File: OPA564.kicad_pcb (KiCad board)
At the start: 2 copper layers, 57.5 x 55 mm, 15 parts, among them IC1 OPA564AIDWD, J1 Conn_Coaxial, J2 Conn_Coaxial

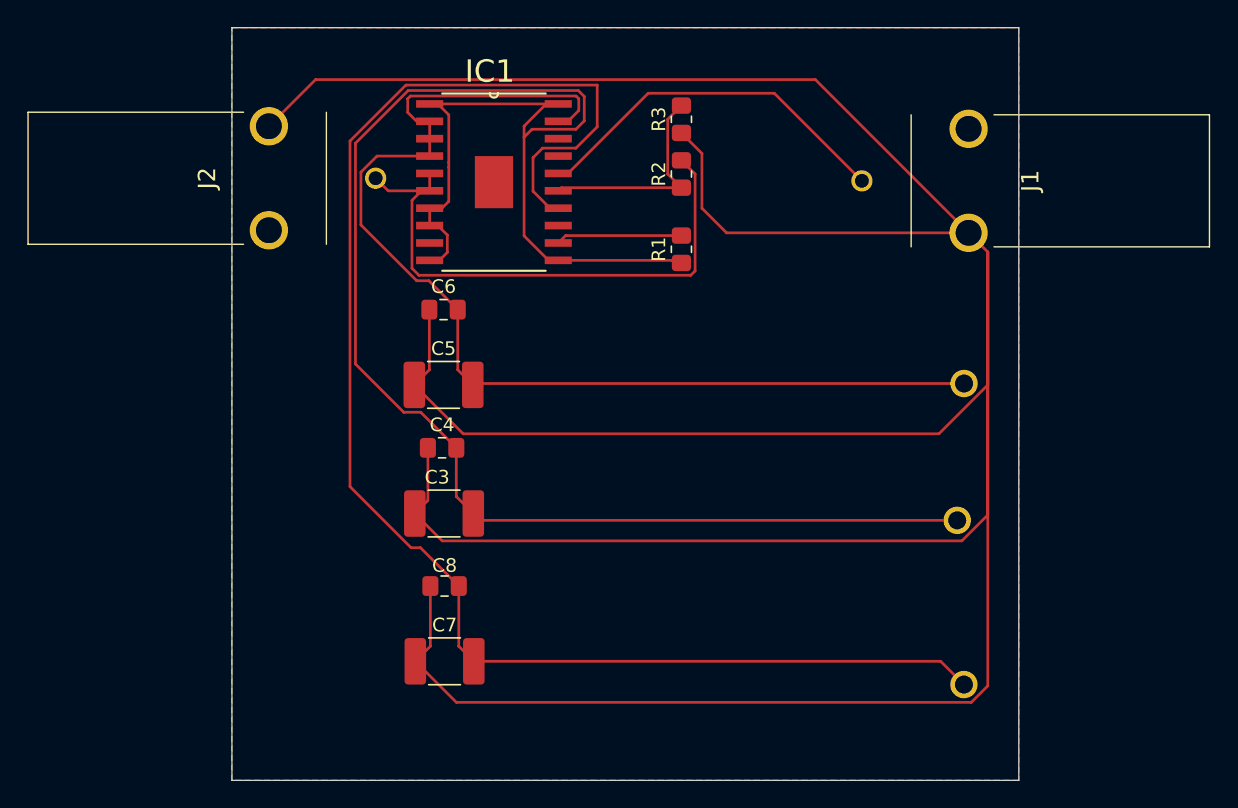
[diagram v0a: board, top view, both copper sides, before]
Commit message: OPA564 simplest design
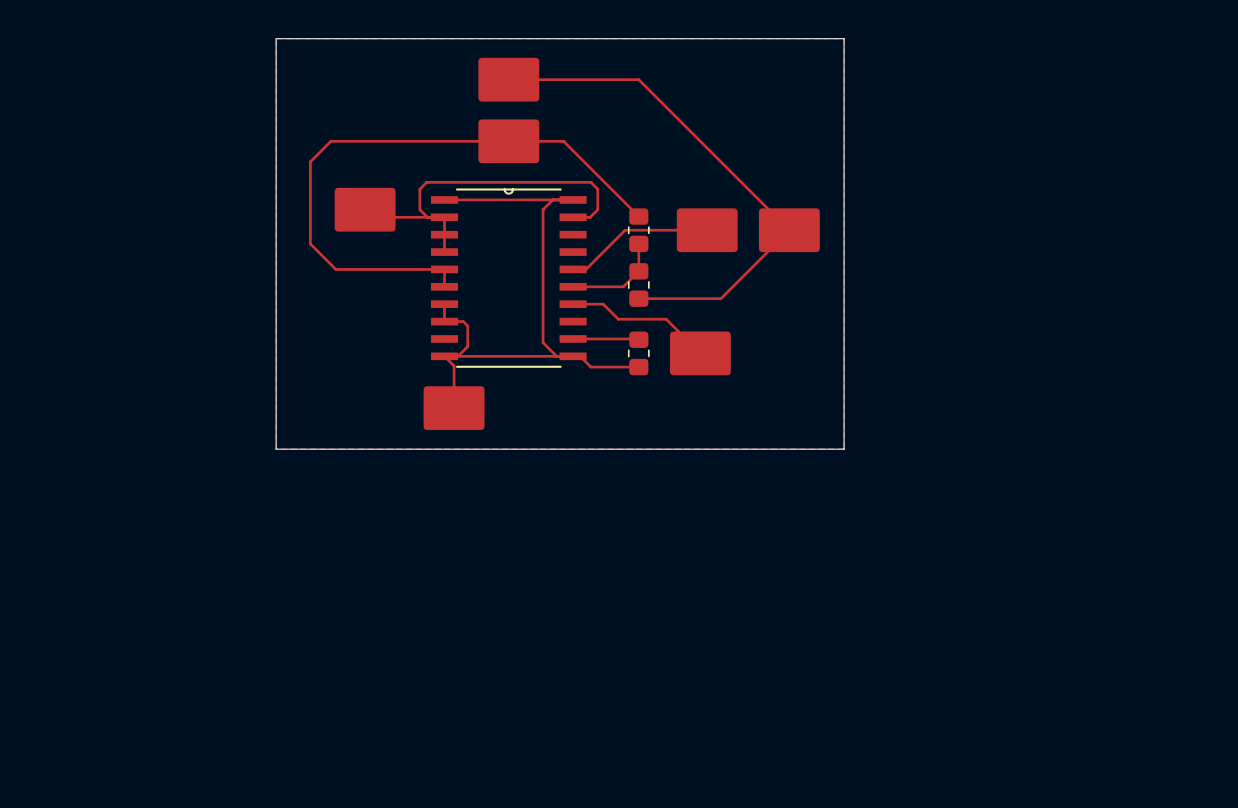
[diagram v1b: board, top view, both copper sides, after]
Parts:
- removed the ? at (169.8, 74.7)
- removed the ? at (169.8, 96.7)
- removed the ? at (169.3, 84.7)
- removed C3, C5, C7: 47 uC, Capacitor_SMD:C_1812_4532Metric_Pad1.57x3.40mm_HandSolder
- removed C4, C6, C8: 0.1 uC, Capacitor_SMD:C_0805_2012Metric_Pad1.18x1.45mm_HandSolder
- removed J1, J2: Conn_Coaxial, 731000154:731000154
- added ?: , , F.Cu at (150.5, 72.5)
- added ?: , , F.Cu at (157.0, 63.5)
- added ?: , , F.Cu at (136.5, 57.0)
- added ?: , , F.Cu at (136.5, 52.5)
- added ?: , , F.Cu at (126.0, 62.0)
- added ?: , , F.Cu at (151.0, 63.5)
- added ?: , , F.Cu at (132.5, 76.5)
- R1: value 14.2 kOhms -> 11 kOhms
- moved R3 12.5 mm to (146.0, 67.5)
- moved R1 8.22 mm to (146.0, 72.5)
- moved IC1 7.10 mm to (136.5, 67.0)
- moved R2 5.16 mm to (146.0, 63.5)
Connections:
- net Net-(IC1-VOUT_1) renamed Signal Output
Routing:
- net GND: track 295.2 -> 38.1 mm
- net -8 Volts: track 111.9 -> 10.8 mm
- net -12 Volts: track 140.9 -> 49.4 mm
- net +12 Volts: track 80.9 -> 29.0 mm
- net Signal Input: track 27.3 -> 11.0 mm
- net Net-(IC1--IN): track 15.9 -> 7.27 mm
- net Net-(IC1-ISET): track 9.22 -> 4.82 mm
- net Signal Output: track 41.7 -> 44.7 mm
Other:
- board size 57.5 x 55 mm -> 41.5 x 30 mm

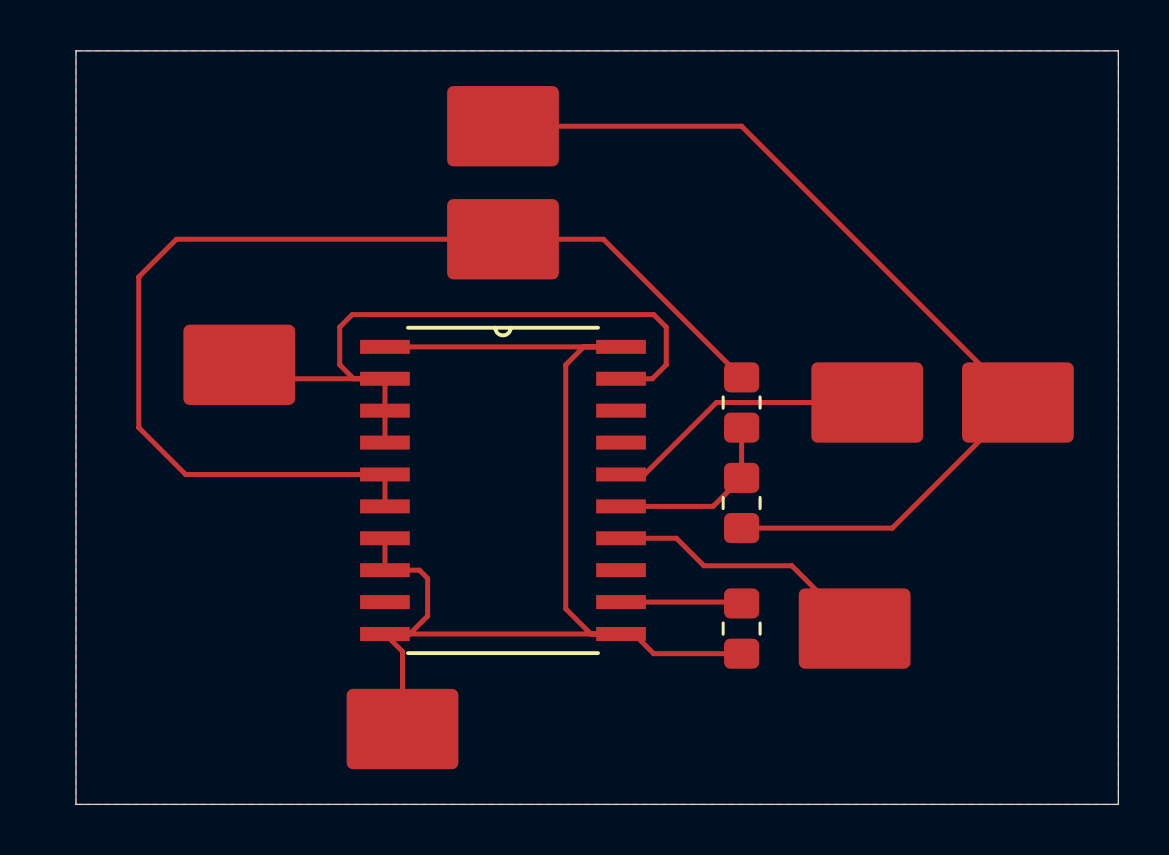
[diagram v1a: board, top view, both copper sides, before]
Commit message: OPA564 Thicker Tracks
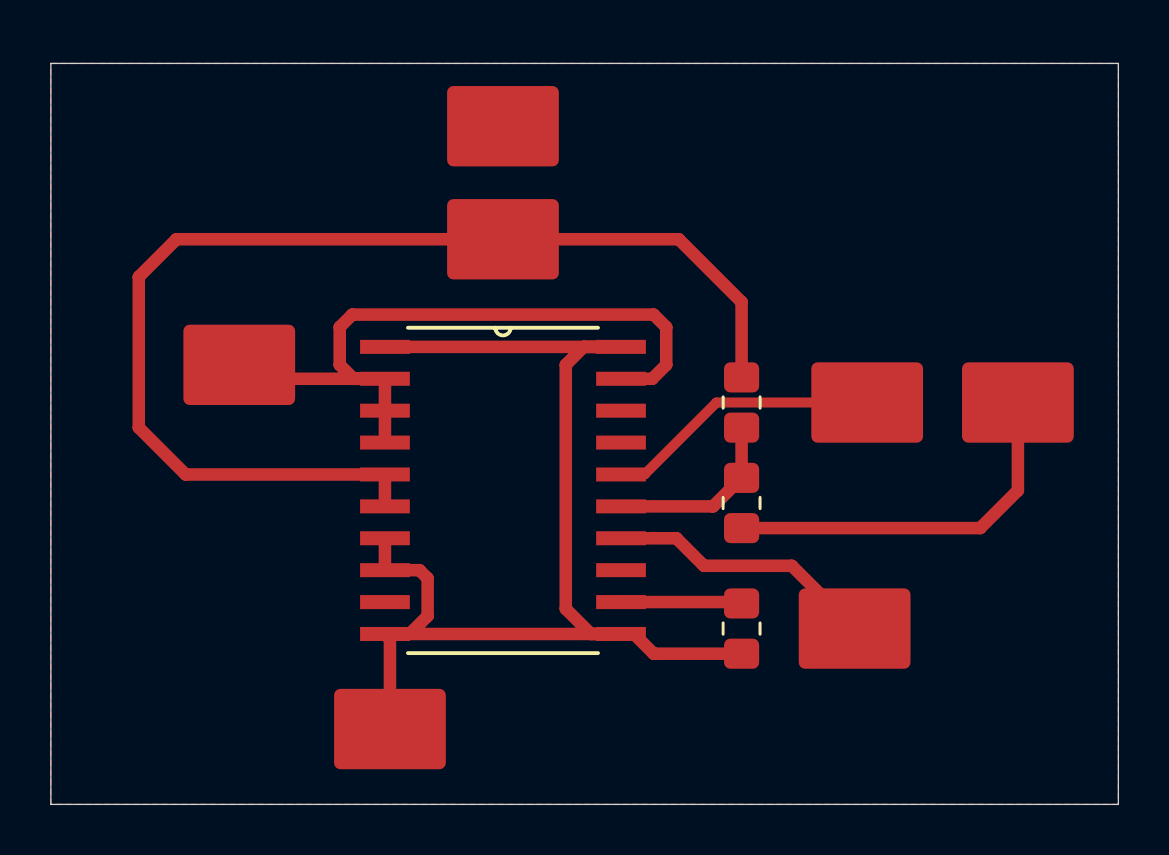
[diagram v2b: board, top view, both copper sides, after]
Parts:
- moved ? 0.50 mm to (132.0, 76.5)
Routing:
- net GND: track 38.1 -> 15.1 mm
- net Signal Output: track 44.7 -> 46.5 mm
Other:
- board size 41.5 x 30 mm -> 42.5 x 29.5 mm
